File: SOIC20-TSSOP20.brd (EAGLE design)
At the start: 22.5 x 27.9 mm, 7 parts

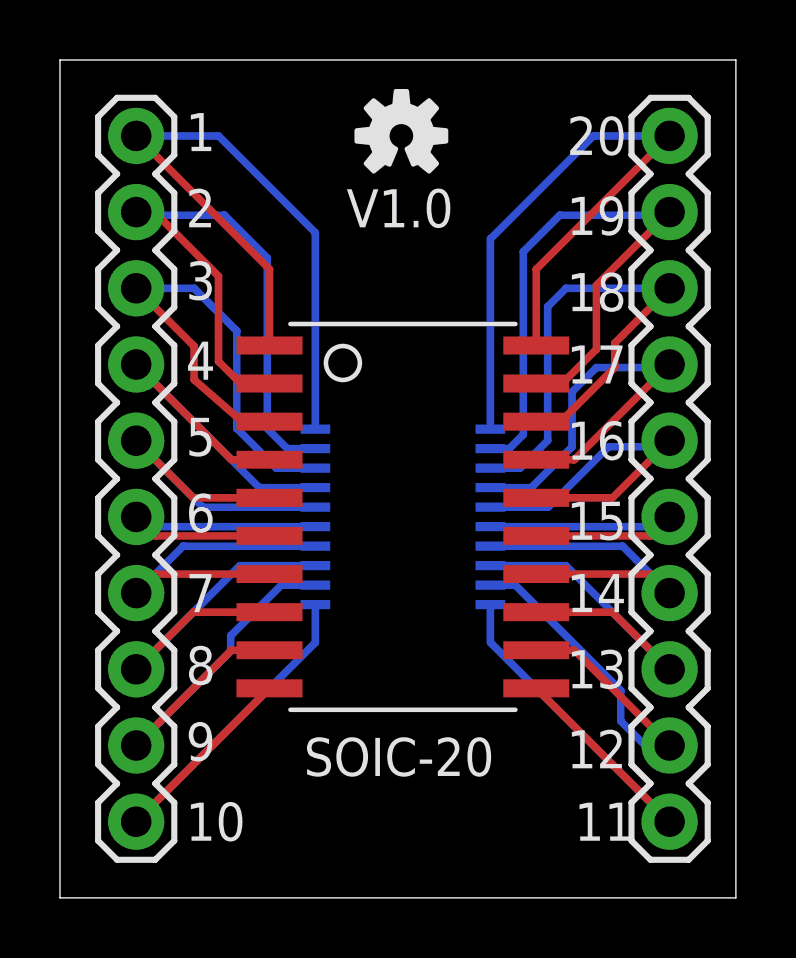
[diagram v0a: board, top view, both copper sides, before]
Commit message: Silk and board revision
Worked several silk screen issues and narrowed some boards.
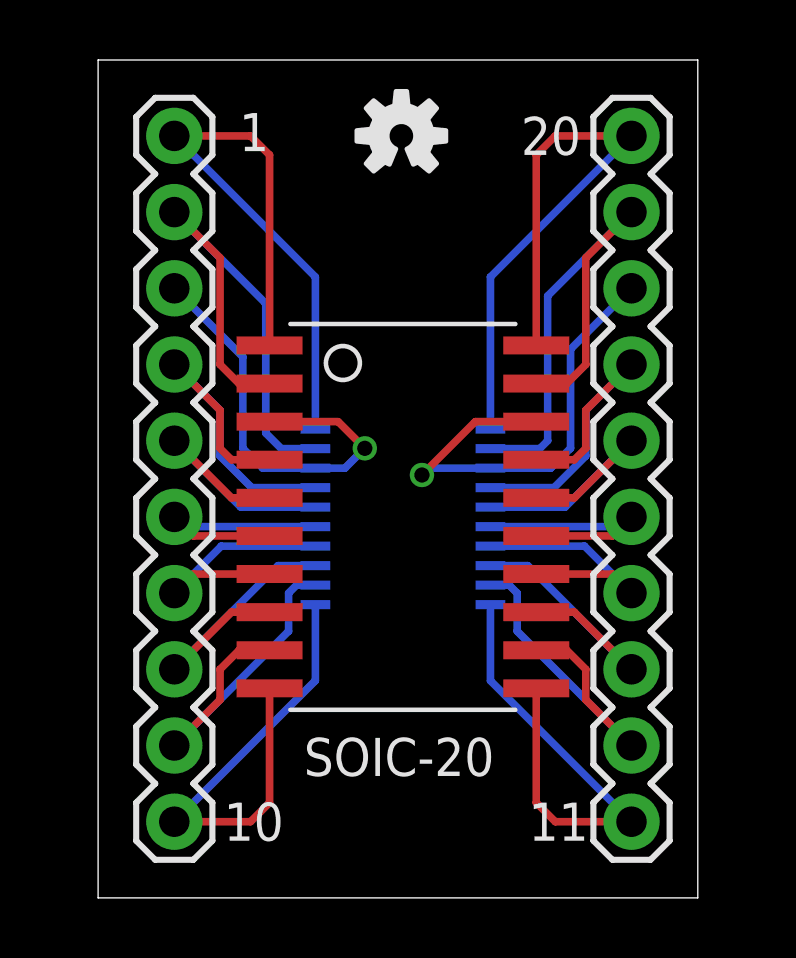
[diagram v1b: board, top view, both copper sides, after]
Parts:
- moved JP1 1.27 mm to (3.81, 2.54)
- moved JP2 1.27 mm to (19.1, 2.54)
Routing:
- net N$2: track 21.1 -> 18.1 mm
- net N$3: track 17.2 -> 14.4 mm, vias 0 -> 1
- net N$8: track 12.6 -> 10.1 mm
- net N$5: track 12.1 -> 9.58 mm
- net N$15: track 12.1 -> 9.58 mm
- net N$7: track 11.3 -> 8.79 mm
- net N$6: track 10.8 -> 8.27 mm
- net N$17: track 11.3 -> 8.79 mm
- net N$16: track 10.8 -> 8.27 mm
- net N$18: track 12.6 -> 10.1 mm
- net N$12: track 20.9 -> 18.4 mm
- net N$14: track 14.5 -> 12.5 mm
- net N$19: track 14.5 -> 12.7 mm
- net N$13: track 17.8 -> 16.2 mm, vias 0 -> 1
- net N$9: track 14.2 -> 12.7 mm
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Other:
- board size 22.5 x 27.9 mm -> 20 x 27.9 mm
- board text removed: "12"
- board text removed: "13"
- board text removed: "14"
- board text removed: "15"
- board text removed: "16"
- board text removed: "17"
- board text removed: "18"
- board text removed: "19"
- board text removed: "2"
- board text removed: "3"
- board text removed: "4"
- board text removed: "5"
- board text removed: "6"
- board text removed: "7"
- board text removed: "8"
- board text removed: "9"
- board text removed: "V1.0"
